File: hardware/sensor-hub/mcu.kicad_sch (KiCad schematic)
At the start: 48 parts, among them J1 Conn_ARM_JTAG_SWD_10, J10 BATT, J2 Micro_SD_Card_Det2, J8 UART_CONN, SW1 SW_Push, U1 STM32F411CEUx, U4 PCAL6408ABS, Y2 32.768kHz, Y3 16MHz

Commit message: Core layout done
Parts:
- removed J2: Micro_SD_Card_Det2, sensor-hub-footprints:MicroSD_Det2, symbol Connector:Micro_SD_Card_Det2
- added J2: Micro_SD_Card_Det2, sensor-hub-footprints:MicroSD_Det2, symbol sensor-hub-lib:Micro_SD_Card_Det2
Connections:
- net +3.3V: now also J2.5 (VDD)
- net CARD_DET: now also J2.10 (DET_A)
- net GND: now also J2.3 (VSS), J2.9 (DET_B), J2.SH (SHIELD)
- net SDIO_CK: now also J2.4 (CLK)
- net SDIO_CMD: now also J2.6 (CMD)
- net SDIO_DAT0: now also J2.2 (DAT0)
- net SDIO_DAT1: now also J2.1 (DAT1)
- net SDIO_DAT2: now also J2.8 (DAT2)
- net SDIO_DAT3: now also J2.7 (DAT3/CD)
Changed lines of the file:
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@@
 	)
 	(junction
-		(at 218.44 71.12)
+		(at 228.6 63.5)
 		(diameter 0)
 		(color 0 0 0 0)
@@
 	)
 	(junction
-		(at 223.52 73.66)
-		(diameter 0)
-		(color 0 0 0 0)
-	)
-	(junction
 		(at 226.06 101.6)
 		(diameter 0)
@@
 	(wire
 		(pts
-			(xy 226.06 63.5) (xy 223.52 63.5)
+			(xy 223.52 63.5) (xy 228.6 63.5)
 		)
 		(stroke
@@
 	(wire
 		(pts
-			(xy 210.82 50.8) (xy 226.06 50.8)
+			(xy 210.82 50.8) (xy 234.95 50.8)
+		)
+		(stroke
+			(width 0)
+			(type default)
+		)
+	)
+	(wire
+		(pts
+			(xy 228.6 63.5) (xy 234.95 63.5)
 		)
 		(stroke
@@
 	(wire
 		(pts
+			(xy 218.44 45.72) (xy 234.95 45.72)
+		)
+		(stroke
+			(width 0)
+			(type default)
+		)
+	)
+	(wire
+		(pts
 			(xy 156.21 130.81) (xy 156.21 133.35)
 		)
@@
 	(wire
 		(pts
-			(xy 149.86 24.13) (xy 140.97 24.13)
+			(xy 234.95 48.26) (xy 228.6 48.26)
 		)
 		(stroke
@@
 	(wire
 		(pts
-			(xy 218.44 43.18) (xy 218.44 71.12)
+			(xy 149.86 24.13) (xy 140.97 24.13)
 		)
 		(stroke
@@
 	(wire
 		(pts
-			(xy 223.52 73.66) (xy 226.06 73.66)
+			(xy 218.44 43.18) (xy 218.44 45.72)
 		)
 		(stroke
@@
 	(wire
 		(pts
-			(xy 218.44 71.12) (xy 226.06 71.12)
-		)
-		(stroke
-			(width 0)
-			(type default)
-		)
-	)
-	(wire
-		(pts
 			(xy 59.69 73.66) (xy 87.63 73.66)
 		)
@@
 	(wire
 		(pts
-			(xy 269.24 73.66) (xy 269.24 78.74)
-		)
-		(stroke
-			(width 0)
-			(type default)
-		)
-	)
-	(wire
-		(pts
 			(xy 86.36 91.44) (xy 87.63 91.44)
 		)
@@
 	(wire
 		(pts
-			(xy 217.17 71.12) (xy 218.44 71.12)
-		)
-		(stroke
-			(width 0)
-			(type default)
-		)
-	)
-	(wire
-		(pts
 			(xy 123.19 81.28) (xy 137.16 81.28)
 		)
@@
 	(wire
 		(pts
-			(xy 223.52 73.66) (xy 223.52 77.47)
-		)
-		(stroke
-			(width 0)
-			(type default)
-		)
-	)
-	(wire
-		(pts
 			(xy 123.19 50.8) (xy 137.16 50.8)
 		)
@@
 	(wire
 		(pts
-			(xy 223.52 63.5) (xy 223.52 73.66)
+			(xy 223.52 63.5) (xy 223.52 77.47)
 		)
 		(stroke
@@
 	(wire
 		(pts
-			(xy 198.12 55.88) (xy 226.06 55.88)
+			(xy 198.12 55.88) (xy 234.95 55.88)
 		)
 		(stroke
@@
 	(wire
 		(pts
-			(xy 179.07 60.96) (xy 226.06 60.96)
+			(xy 179.07 60.96) (xy 234.95 60.96)
 		)
 		(stroke
@@
 	(wire
 		(pts
+			(xy 278.13 72.39) (xy 278.13 77.47)
+		)
+		(stroke
+			(width 0)
+			(type default)
+		)
+	)
+	(wire
+		(pts
 			(xy 243.84 146.05) (xy 243.84 137.16)
 		)
@@
 	(wire
 		(pts
-			(xy 185.42 66.04) (xy 226.06 66.04)
+			(xy 185.42 66.04) (xy 234.95 66.04)
 		)
 		(stroke
@@
 	(wire
 		(pts
-			(xy 226.06 58.42) (xy 223.52 58.42)
+			(xy 223.52 58.42) (xy 234.95 58.42)
 		)
 		(stroke
@@
 	(wire
 		(pts
-			(xy 204.47 53.34) (xy 226.06 53.34)
+			(xy 204.47 53.34) (xy 234.95 53.34)
 		)
 		(stroke
@@
 	(wire
 		(pts
-			(xy 191.77 68.58) (xy 226.06 68.58)
+			(xy 191.77 68.58) (xy 234.95 68.58)
 		)
 		(stroke
@@
 		)
 	)
+	(wire
+		(pts
+			(xy 228.6 48.26) (xy 228.6 63.5)
+		)
+		(stroke
+			(width 0)
+			(type default)
+		)
+	)
 	(text "BOOT[1:0]:\nx0 - Flash\n01 - Bootloader\n11 - SRAM\n"
 		(exclude_from_sim no)
@@
 	)
 	(label "CARD_DET"
-		(at 217.17 71.12 180)
+		(at 224.79 45.72 0)
 		(effects
 			(font
 				(size 1.27 1.27)
 			)
-			(justify right bottom)
+			(justify left bottom)
 		)
 	)
@@
 	(symbol
 		(lib_id "power:GND")
-		(at 269.24 78.74 0)
+		(at 278.13 77.47 0)
 		(unit 1)
 		(exclude_from_sim no)
@@
 		(dnp no)
 		(property "Reference" "#PWR51"
-			(at 269.24 85.09 0)
+			(at 278.13 83.82 0)
 			(effects
 				(font
@@
 		)
 		(property "Value" "GND"
-			(at 265.43 80.518 0)
+			(at 274.32 79.248 0)
 			(effects
 				(font
@@
 		)
 		(property "Footprint" ""
-			(at 269.24 78.74 0)
+			(at 278.13 77.47 0)
 			(effects
 				(font
@@
 		)
 		(property "Datasheet" ""
-			(at 269.24 78.74 0)
+			(at 278.13 77.47 0)
 			(effects
 				(font
@@
 		)
 		(property "Description" "Power symbol creates a global label with name \"GND\" , ground"
-			(at 269.24 78.74 0)
+			(at 278.13 77.47 0)
 			(effects
 				(font
@@
 	)
 	(symbol
-		(lib_id "Connector:Micro_SD_Card_Det2")
-		(at 248.92 60.96 0)
-		(unit 1)
-		(exclude_from_sim no)
-		(in_bom yes)
-		(on_board yes)
-		(dnp no)
-		(fields_autoplaced yes)
-		(property "Reference" "J2"
-			(at 249.555 39.37 0)
-			(effects
-				(font
-					(size 1.27 1.27)
-				)
-			)
-		)
-		(property "Value" "Micro_SD_Card_Det2"
-			(at 249.555 41.91 0)
-			(effects
-				(font
-					(size 1.27 1.27)
-				)
-			)
-		)
-		(property "Footprint" "sensor-hub-footprints:MicroSD_Det2"
-			(at 300.99 43.18 0)
-			(effects
-				(font
-					(size 1.27 1.27)
-				)
-				(hide yes)
-			)
-		)
-		(property "Datasheet" "https://www.hirose.com/en/product/document?clcode=&productname=&series=DM3&documenttype=Catalog&lang=en&documentid=D49662_en"
-			(at 251.46 58.42 0)
-			(effects
-				(font
-					(size 1.27 1.27)
-				)
-				(hide yes)
-			)
-		)
-		(property "Description" "Micro SD Card Socket with two card detection pins"
-			(at 248.92 60.96 0)
-			(effects
-				(font
-					(size 1.27 1.27)
-				)
-				(hide yes)
-			)
-		)
-		(pin "5"
-		)
-		(pin "7"
-		)
-		(pin "10"
-		)
-		(pin "1"
-		)
-		(pin "8"
-		)
-		(pin "9"
-		)
-		(pin "4"
-		)
-		(pin "11"
-		)
-		(pin "3"
-		)
-		(pin "2"
-		)
-		(pin "6"
-		)
-		(instances
-			(project ""
-				(path "/e168ef7b-16e4-493f-b63c-2f69374fc890/acb07f68-122e-4e37-938b-04e6ced67923"
-					(reference "J2")
-					(unit 1)
-				)
-			)
-		)
-	)
-	(symbol
 		(lib_id "power:GND")
 		(at 35.56 39.37 0)
@@
 					(unit 1)
 				)
+			)
+		)
+	)
+	(symbol
+		(lib_id "sensor-hub-lib:Micro_SD_Card_Det2")
+		(at 257.81 59.69 0)
+		(unit 1)
+		(exclude_from_sim no)
+		(in_bom yes)
+		(on_board yes)
+		(dnp no)
+		(fields_autoplaced yes)
+		(property "Reference" "J2"
+			(at 258.445 38.1 0)
+			(effects
+				(font
+					(size 1.27 1.27)
+				)
+			)
+		)
+		(property "Value" "Micro_SD_Card_Det2"
+			(at 258.445 40.64 0)
+			(effects
+				(font
+					(size 1.27 1.27)
+				)
+			)
+		)
+		(property "Footprint" "sensor-hub-footprints:MicroSD_Det2"
+			(at 309.88 41.91 0)
+			(effects
+				(font
+					(size 1.27 1.27)
+				)
+				(hide yes)
+			)
+		)
+		(property "Datasheet" ""
+			(at 260.35 57.15 0)
+			(effects
+				(font
+					(size 1.27 1.27)
+				)
+				(hide yes)
+			)
+		)
+		(property "Description" "Micro SD Card Socket with two card detection pins"
+			(at 257.81 59.69 0)
+			(effects
+				(font
+					(size 1.27 1.27)
+				)
+				(hide yes)
+			)
+		)
+		(pin "1"
+		)
+		(pin "5"
+		)
+		(pin "8"
+		)
+		(pin "10"
+		)
+		(pin "2"
+		)
+		(pin "6"
+		)
+		(pin "7"
+		)
+		(pin "4"
+		)
+		(pin "3"
+		)
+		(pin "9"
+		)
+		(pin "SH"
+		)
+		(instances
+			(project ""
+				(path "/e168ef7b-16e4-493f-b63c-2f69374fc890/acb07f68-122e-4e37-938b-04e6ced67923"
+					(reference "J2")
+					(unit 1)
+				)

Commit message: Most layout done
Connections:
- net CARD_DET: now also U4.7 (P4); no longer U4.10 (P7)
- net at R21.1: now also U4.8 (P5); no longer U4.7 (P4)
- net at R22.1: now also U4.9 (P6); no longer U4.8 (P5)
- net at R23.1: now also U4.10 (P7); no longer U4.9 (P6)
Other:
- moved on the sheet: D1, R21, R22, R23
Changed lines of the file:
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@@
 	(wire
 		(pts
+			(xy 208.28 125.73) (xy 210.82 125.73)
+		)
+		(stroke
+			(width 0)
+			(type default)
+		)
+	)
+	(wire
+		(pts
 			(xy 248.92 118.11) (xy 248.92 132.08)
 		)
@@
 	(wire
 		(pts
-			(xy 227.33 148.59) (xy 227.33 149.86)
+			(xy 227.33 151.13) (xy 227.33 152.4)
 		)
 		(stroke
@@
 	(wire
 		(pts
-			(xy 208.28 125.73) (xy 232.41 125.73)
+			(xy 208.28 128.27) (xy 232.41 128.27)
 		)
 		(stroke
@@
 	(wire
 		(pts
-			(xy 208.28 133.35) (xy 210.82 133.35)
-		)
-		(stroke
-			(width 0)
-			(type default)
-		)
-	)
-	(wire
-		(pts
-			(xy 227.33 128.27) (xy 227.33 133.35)
+			(xy 227.33 130.81) (xy 227.33 135.89)
 		)
 		(stroke
@@
 	(wire
 		(pts
-			(xy 208.28 128.27) (xy 227.33 128.27)
+			(xy 208.28 130.81) (xy 227.33 130.81)
 		)
 		(stroke
@@
 	(wire
 		(pts
-			(xy 232.41 125.73) (xy 232.41 133.35)
+			(xy 232.41 128.27) (xy 232.41 135.89)
 		)
 		(stroke
@@
 	(wire
 		(pts
-			(xy 222.25 133.35) (xy 222.25 130.81)
+			(xy 222.25 135.89) (xy 222.25 133.35)
 		)
 		(stroke
@@
 	(wire
 		(pts
-			(xy 222.25 130.81) (xy 208.28 130.81)
+			(xy 222.25 133.35) (xy 208.28 133.35)
 		)
 		(stroke
@@
 	)
 	(label "CARD_DET"
-		(at 210.82 133.35 0)
+		(at 210.82 125.73 0)
 		(effects
 			(font
@@
 	(symbol
 		(lib_id "Device:R_Small")
-		(at 227.33 135.89 0)
+		(at 227.33 138.43 0)
 		(unit 1)
 		(exclude_from_sim no)
@@
 		(dnp no)
 		(property "Reference" "R22"
-			(at 229.108 137.922 90)
+			(at 229.108 140.462 90)
 			(effects
 				(font
@@
 		)
 		(property "Value" "4.7k"
-			(at 225.552 137.922 90)
+			(at 225.552 140.462 90)
 			(effects
 				(font
@@
 		)
 		(property "Footprint" "Resistor_SMD:R_0603_1608Metric"
-			(at 227.33 135.89 0)
+			(at 227.33 138.43 0)
 			(effects
 				(font
@@
 		)
 		(property "Datasheet" "~"
-			(at 227.33 135.89 0)
+			(at 227.33 138.43 0)
 			(effects
 				(font
@@
 		)
 		(property "Description" "Resistor, small symbol"
-			(at 227.33 135.89 0)
+			(at 227.33 138.43 0)
 			(effects
 				(font
@@
 	(symbol
 		(lib_id "power:GND")
-		(at 227.33 149.86 0)
+		(at 227.33 152.4 0)
 		(unit 1)
 		(exclude_from_sim no)
@@
 		(fields_autoplaced yes)
 		(property "Reference" "#PWR54"
-			(at 227.33 156.21 0)
+			(at 227.33 158.75 0)
 			(effects
 				(font
@@
 		)
 		(property "Value" "GND"
-			(at 227.33 154.94 0)
+			(at 227.33 157.48 0)
 			(effects
 				(font
@@
 		)
 		(property "Footprint" ""
-			(at 227.33 149.86 0)
+			(at 227.33 152.4 0)
 			(effects
 				(font
@@
 		)
 		(property "Datasheet" ""
-			(at 227.33 149.86 0)
+			(at 227.33 152.4 0)
 			(effects
 				(font
@@
 		)
 		(property "Description" "Power symbol creates a global label with name \"GND\" , ground"
-			(at 227.33 149.86 0)
+			(at 227.33 152.4 0)
 			(effects
 				(font
@@
 	(symbol
 		(lib_id "Device:R_Small")
-		(at 222.25 135.89 0)
+		(at 222.25 138.43 0)
 		(unit 1)
 		(exclude_from_sim no)
@@
 		(dnp no)
 		(property "Reference" "R23"
-			(at 224.028 137.922 90)
+			(at 224.028 140.462 90)
 			(effects
 				(font
@@
 		)
 		(property "Value" "4.7k"
-			(at 220.472 137.922 90)
+			(at 220.472 140.462 90)
 			(effects
 				(font
@@
 		)
 		(property "Footprint" "Resistor_SMD:R_0603_1608Metric"
-			(at 222.25 135.89 0)
+			(at 222.25 138.43 0)
 			(effects
 				(font
@@
 		)
 		(property "Datasheet" "~"
-			(at 222.25 135.89 0)
+			(at 222.25 138.43 0)
 			(effects
 				(font
@@
 		)
 		(property "Description" "Resistor, small symbol"
-			(at 222.25 135.89 0)
+			(at 222.25 138.43 0)
 			(effects
 				(font
@@
 	(symbol
 		(lib_id "Device:LED_BGKR")
-		(at 227.33 143.51 90)
+		(at 227.33 146.05 90)
 		(unit 1)
 		(exclude_from_sim no)
@@
 		(dnp no)
 		(property "Reference" "D1"
-			(at 216.154 141.478 90)
+			(at 216.154 144.018 90)
 			(effects
 				(font
@@
 		)
 		(property "Value" "LED_BGKR"
-			(at 209.042 145.542 90)
+			(at 209.042 148.082 90)
 			(effects
 				(font
@@
 		)
 		(property "Footprint" "LED_SMD:LED_Cree-PLCC4_3.2x2.8mm_CCW"
-			(at 228.6 143.51 0)
+			(at 228.6 146.05 0)
 			(effects
 				(font
@@
 		)
 		(property "Datasheet" "~"
-			(at 228.6 143.51 0)
+			(at 228.6 146.05 0)
 			(effects
 				(font
@@
 		)
 		(property "Description" "RGB LED, blue/green/cathode/red"
-			(at 227.33 143.51 0)
+			(at 227.33 146.05 0)
 			(effects
 				(font
@@
 	(symbol
 		(lib_id "Device:R_Small")
-		(at 232.41 135.89 0)
+		(at 232.41 138.43 0)
 		(unit 1)
 		(exclude_from_sim no)
@@
 		(dnp no)
 		(property "Reference" "R21"
-			(at 234.188 137.922 90)
+			(at 234.188 140.462 90)
 			(effects
 				(font
@@
 		)
 		(property "Value" "4.7k"
-			(at 230.632 137.922 90)
+			(at 230.632 140.462 90)
 			(effects
 				(font
@@
 		)
 		(property "Footprint" "Resistor_SMD:R_0603_1608Metric"
-			(at 232.41 135.89 0)
+			(at 232.41 138.43 0)
 			(effects
 				(font
@@
 		)
 		(property "Datasheet" "~"
-			(at 232.41 135.89 0)
+			(at 232.41 138.43 0)
 			(effects
 				(font
@@
 		)
 		(property "Description" "Resistor, small symbol"
-			(at 232.41 135.89 0)
+			(at 232.41 138.43 0)
 			(effects
 				(font

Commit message: DRC fixes
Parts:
- removed D1: LED_BGKR, LED_SMD:LED_Cree-PLCC4_3.2x2.8mm_CCW, symbol Device:LED_BGKR
- added D1: LED_BGRA, LED_SMD:LED_Cree-PLCC4_3.2x2.8mm_CCW, symbol Device:LED_BGRA
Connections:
- net +3.3V: now also D1.4 (A)
- net at R22.2: now also D1.2 (GK)
- net at R23.2: now also D1.1 (BK)
- net at R21.2: now also D1.3 (RK)
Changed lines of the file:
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@@
 	(wire
 		(pts
+			(xy 227.33 153.67) (xy 207.01 153.67)
+		)
+		(stroke
+			(width 0)
+			(type default)
+		)
+	)
+	(wire
+		(pts
 			(xy 60.96 55.88) (xy 59.69 55.88)
 		)
@@
 	(wire
 		(pts
-			(xy 227.33 151.13) (xy 227.33 152.4)
+			(xy 227.33 151.13) (xy 227.33 153.67)
 		)
 		(stroke
@@
 	(wire
 		(pts
+			(xy 207.01 153.67) (xy 207.01 148.59)
+		)
+		(stroke
+			(width 0)
+			(type default)
+		)
+	)
+	(wire
+		(pts
 			(xy 185.42 43.18) (xy 185.42 66.04)
 		)
@@
 	)
 	(symbol
+		(lib_id "Device:LED_BGRA")
+		(at 227.33 146.05 270)
+		(unit 1)
+		(exclude_from_sim no)
+		(in_bom yes)
+		(on_board yes)
+		(dnp no)
+		(property "Reference" "D1"
+			(at 216.916 144.018 90)
+			(effects
+				(font
+					(size 1.27 1.27)
+				)
+				(justify left)
+			)
+		)
+		(property "Value" "LED_BGRA"
+			(at 209.804 148.082 90)
+			(effects
+				(font
+					(size 1.27 1.27)
+				)
+				(justify left)
+			)
+		)
+		(property "Footprint" "LED_SMD:LED_Cree-PLCC4_3.2x2.8mm_CCW"
+			(at 226.06 146.05 0)
+			(effects
+				(font
+					(size 1.27 1.27)
+				)
+				(hide yes)
+			)
+		)
+		(property "Datasheet" "~"
+			(at 226.06 146.05 0)
+			(effects
+				(font
+					(size 1.27 1.27)
+				)
+				(hide yes)
+			)
+		)
+		(property "Description" "RGB LED, blue/green/red/anode"
+			(at 227.33 146.05 0)
+			(effects
+				(font
+					(size 1.27 1.27)
+				)
+				(hide yes)
+			)
+		)
+		(pin "1"
+		)
+		(pin "2"
+		)
+		(pin "4"
+		)
+		(pin "3"
+		)
+		(instances
+			(project ""
+				(path "/e168ef7b-16e4-493f-b63c-2f69374fc890/acb07f68-122e-4e37-938b-04e6ced67923"
+					(reference "D1")
+					(unit 1)
+				)
+			)
+		)
+	)
+	(symbol
 		(lib_id "Device:C_Small")
 		(at 170.18 27.94 0)
@@
 	)
 	(symbol
-		(lib_id "power:GND")
-		(at 227.33 152.4 0)
+		(lib_id "Device:R_Small")
+		(at 198.12 40.64 0)
 		(unit 1)
 		(exclude_from_sim no)
@@
 		(on_board yes)
 		(dnp no)
-		(fields_autoplaced yes)
-		(property "Reference" "#PWR54"
-			(at 227.33 158.75 0)
+		(property "Reference" "R17"
+			(at 198.882 39.116 0)
 			(effects
 				(font
 					(size 1.27 1.27)
 				)
-				(hide yes)
+				(justify left)
 			)
 		)
-		(property "Value" "GND"
-			(at 227.33 157.48 0)
+		(property "Value" "47k"
+			(at 199.136 41.91 0)
 			(effects
 				(font
 					(size 1.27 1.27)
 				)
+				(justify left)
 			)
 		)
-		(property "Footprint" ""
-			(at 227.33 152.4 0)
+		(property "Footprint" "Resistor_SMD:R_0603_1608Metric"
+			(at 198.12 40.64 0)
 			(effects
 				(font
@@
 			)
 		)
-		(property "Datasheet" ""
-			(at 227.33 152.4 0)
+		(property "Datasheet" "~"
+			(at 198.12 40.64 0)
 			(effects
 				(font
@@
 			)
 		)
-		(property "Description" "Power symbol creates a global label with name \"GND\" , ground"
-			(at 227.33 152.4 0)
+		(property "Description" "Resistor, small symbol"
+			(at 198.12 40.64 0)
 			(effects
 				(font
@@
 		(pin "1"
 		)
+		(pin "2"
+		)
 		(instances
 			(project "sensor-hub"
 				(path "/e168ef7b-16e4-493f-b63c-2f69374fc890/acb07f68-122e-4e37-938b-04e6ced67923"
-					(reference "#PWR54")
+					(reference "R17")
 					(unit 1)
 				)
@@
 	)
 	(symbol
-		(lib_id "Device:R_Small")
-		(at 198.12 40.64 0)
+		(lib_id "power:+3.3V")
+		(at 207.01 148.59 0)
 		(unit 1)
 		(exclude_from_sim no)
@@
 		(on_board yes)
 		(dnp no)
-		(property "Reference" "R17"
-			(at 198.882 39.116 0)
+		(fields_autoplaced yes)
+		(property "Reference" "#PWR54"
+			(at 207.01 152.4 0)
 			(effects
 				(font
 					(size 1.27 1.27)
 				)
-				(justify left)
+				(hide yes)
 			)
 		)
-		(property "Value" "47k"
-			(at 199.136 41.91 0)
+		(property "Value" "+3.3V"
+			(at 207.01 143.51 0)
 			(effects
 				(font
 					(size 1.27 1.27)
 				)
-				(justify left)
 			)
 		)
-		(property "Footprint" "Resistor_SMD:R_0603_1608Metric"
-			(at 198.12 40.64 0)
+		(property "Footprint" ""
+			(at 207.01 148.59 0)
 			(effects
 				(font
@@
 			)
 		)
-		(property "Datasheet" "~"
-			(at 198.12 40.64 0)
+		(property "Datasheet" ""
+			(at 207.01 148.59 0)
 			(effects
 				(font
@@
 			)
 		)
-		(property "Description" "Resistor, small symbol"
-			(at 198.12 40.64 0)
+		(property "Description" "Power symbol creates a global label with name \"+3.3V\""
+			(at 207.01 148.59 0)
 			(effects
 				(font
@@
 		(pin "1"
 		)
-		(pin "2"
-		)
 		(instances
 			(project "sensor-hub"
 				(path "/e168ef7b-16e4-493f-b63c-2f69374fc890/acb07f68-122e-4e37-938b-04e6ced67923"
-					(reference "R17")
+					(reference "#PWR54")
 					(unit 1)
 				)
@@
 					(unit 1)
 				)
-			)
-		)
-	)
-	(symbol
-		(lib_id "Device:LED_BGKR")
-		(at 227.33 146.05 90)
-		(unit 1)
-		(exclude_from_sim no)
-		(in_bom yes)
-		(on_board yes)
-		(dnp no)
-		(property "Reference" "D1"
-			(at 216.154 144.018 90)
-			(effects
-				(font
-					(size 1.27 1.27)
-				)
-				(justify right)
-			)
-		)
-		(property "Value" "LED_BGKR"
-			(at 209.042 148.082 90)
-			(effects
-				(font
-					(size 1.27 1.27)
-				)
-				(justify right)
-			)
-		)
-		(property "Footprint" "LED_SMD:LED_Cree-PLCC4_3.2x2.8mm_CCW"
-			(at 228.6 146.05 0)
-			(effects
-				(font
-					(size 1.27 1.27)
-				)
-				(hide yes)
-			)
-		)
-		(property "Datasheet" "~"
-			(at 228.6 146.05 0)
-			(effects
-				(font
-					(size 1.27 1.27)
-				)
-				(hide yes)
-			)
-		)
-		(property "Description" "RGB LED, blue/green/cathode/red"
-			(at 227.33 146.05 0)
-			(effects
-				(font
-					(size 1.27 1.27)
-				)
-				(hide yes)
-			)
-		)
-		(pin "1"
-		)
-		(pin "4"
-		)
-		(pin "2"
-		)
-		(pin "3"
-		)
-		(instances
-			(project ""
-				(path "/e168ef7b-16e4-493f-b63c-2f69374fc890/acb07f68-122e-4e37-938b-04e6ced67923"
-					(reference "D1")
-					(unit 1)
-				)

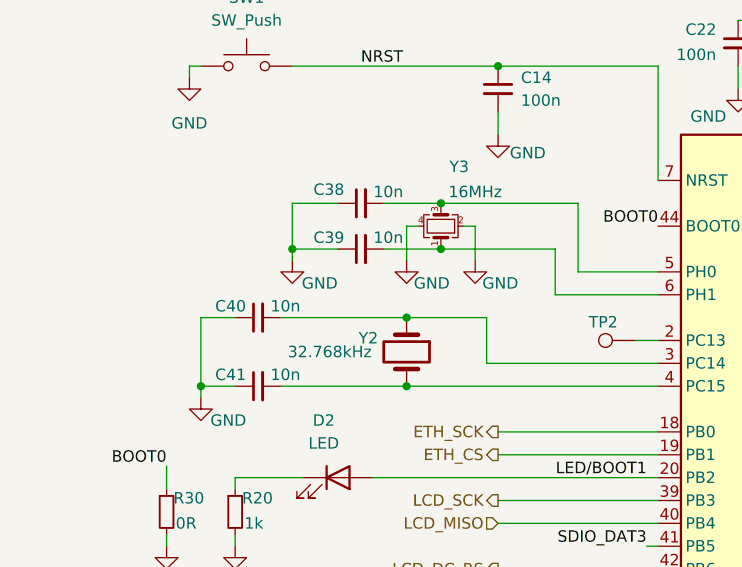
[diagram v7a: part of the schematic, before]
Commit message: V1.0
Fixed value typos, replaced vias with 0.3/0.45, added production files
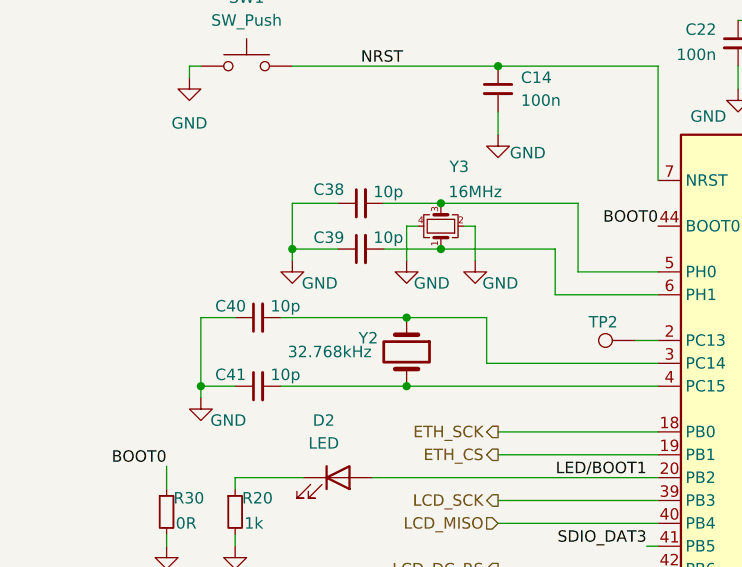
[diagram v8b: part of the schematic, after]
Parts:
- C38, C39, C40, C41: value 10n -> 10p
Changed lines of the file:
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@@
 			)
 		)
-		(property "Value" "10n"
+		(property "Value" "10p"
 			(at 57.658 52.07 90)
 			(effects
@@
 			)
 		)
-		(property "Value" "10n"
+		(property "Value" "10p"
 			(at 46.228 64.77 90)
 			(effects
@@
 			)
 		)
-		(property "Value" "10n"
+		(property "Value" "10p"
 			(at 46.228 72.39 90)
 			(effects
@@
 			)
 		)
-		(property "Value" "10n"
+		(property "Value" "10p"
 			(at 57.658 57.15 90)
 			(effects
